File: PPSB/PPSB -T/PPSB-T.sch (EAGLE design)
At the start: 7 parts, among them U1 DS18B20

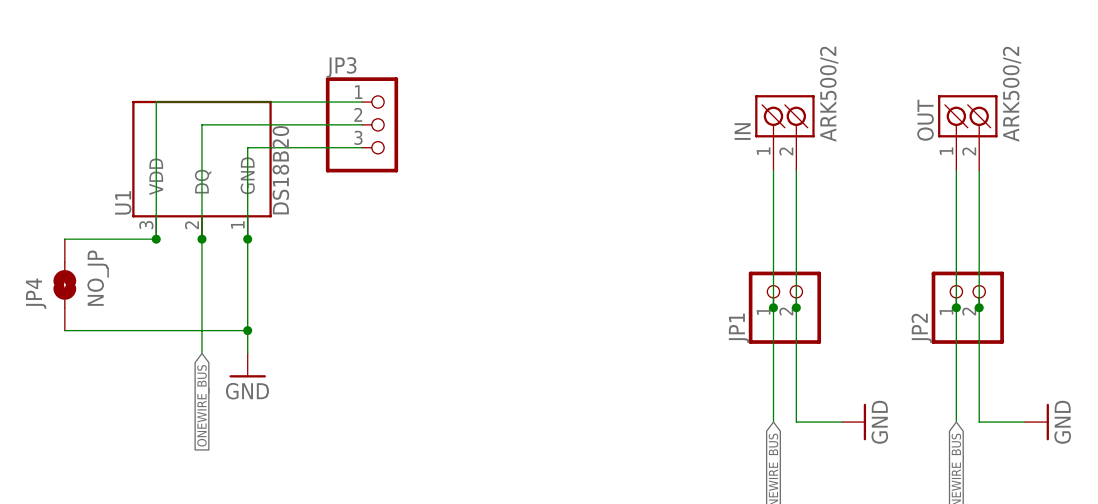
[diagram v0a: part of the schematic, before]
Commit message: Remove obsolete files, pre-release versions of PPSB-T & PPSB-TH
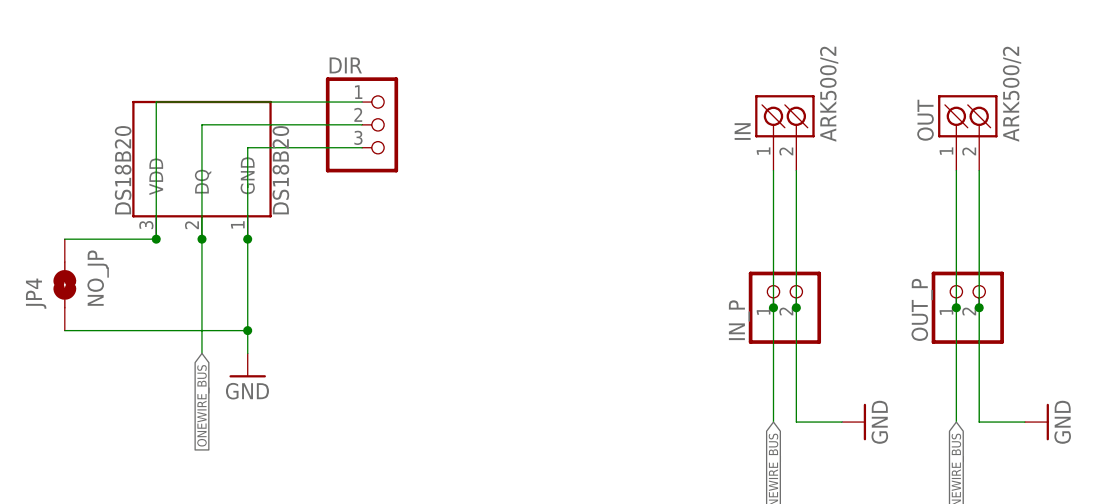
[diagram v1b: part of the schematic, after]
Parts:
- renumbered JP1 to IN_P, JP2 to OUT_P, JP3 to DIR, U1 to DS18B20
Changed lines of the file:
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@@
 <?xml version="1.0" encoding="utf-8"?>
 <!DOCTYPE eagle SYSTEM "eagle.dtd">
-<eagle version="9.5.2">
+<eagle version="9.6.1">
 <drawing>
 <settings>
@@
 <setting verticaltext="up"/>
 </settings>
-<grid distance="0.1" unitdist="inch" unit="inch" style="lines" multiple="1" display="yes" altdistance="0.01" altunitdist="inch" altunit="inch"/>
+<grid distance="0.1" unitdist="inch" unit="inch" style="lines" multiple="1" display="no" altdistance="0.01" altunitdist="inch" altunit="inch"/>
 <layers>
 <layer number="1" name="Top" color="4" fill="1" visible="no" active="no"/>
@@
 <parts>
 <part name="FRAME1" library="frames" library_urn="urn:adsk.eagle:library:229" deviceset="A4L-LOC" device=""/>
-<part name="U1" library="SparkFun-Sensors" deviceset="DS18B20" device=""/>
+<part name="DS18B20" library="SparkFun-Sensors" deviceset="DS18B20" device=""/>
 <part name="GND1" library="supply1" library_urn="urn:adsk.eagle:library:371" deviceset="GND" device=""/>
 <part name="IN" library="#PaJa_konektory" deviceset="ARK500/2" device=""/>
 <part name="OUT" library="#PaJa_konektory" deviceset="ARK500/2" device=""/>
-<part name="JP1" library="pinhead" library_urn="urn:adsk.eagle:library:325" deviceset="PINHD-1X2" device="" package3d_urn="urn:adsk.eagle:package:22435/2"/>
-<part name="JP2" library="pinhead" library_urn="urn:adsk.eagle:library:325" deviceset="PINHD-1X2" device="" package3d_urn="urn:adsk.eagle:package:22435/2"/>
+<part name="IN_P" library="pinhead" library_urn="urn:adsk.eagle:library:325" deviceset="PINHD-1X2" device="" package3d_urn="urn:adsk.eagle:package:22435/2"/>
+<part name="OUT_P" library="pinhead" library_urn="urn:adsk.eagle:library:325" deviceset="PINHD-1X2" device="" package3d_urn="urn:adsk.eagle:package:22435/2"/>
 <part name="GND3" library="supply1" library_urn="urn:adsk.eagle:library:371" deviceset="GND" device=""/>
 <part name="GND2" library="supply1" library_urn="urn:adsk.eagle:library:371" deviceset="GND" device=""/>
-<part name="JP3" library="pinhead" library_urn="urn:adsk.eagle:library:325" deviceset="PINHD-1X3" device="" package3d_urn="urn:adsk.eagle:package:22458/2"/>
+<part name="DIR" library="pinhead" library_urn="urn:adsk.eagle:library:325" deviceset="PINHD-1X3" device="" package3d_urn="urn:adsk.eagle:package:22458/2"/>
 <part name="JP4" library="SparkFun-Jumpers" deviceset="JUMPER-SMT_2_NO" device="_NO-SILK" package3d_urn="urn:adsk.eagle:package:39277/1" value="NO_JP"/>
 </parts>
@@
 <attribute name="SHEET" x="230.505" y="5.08" size="2.54" layer="94"/>
 </instance>
-<instance part="U1" gate="G$1" x="58.42" y="134.62" smashed="yes" rot="R90">
+<instance part="DS18B20" gate="G$1" x="58.42" y="134.62" smashed="yes" rot="R90">
 <attribute name="NAME" x="50.546" y="127" size="1.778" layer="95" font="vector" rot="R90"/>
 <attribute name="VALUE" x="66.294" y="127" size="1.778" layer="96" font="vector" rot="R90" align="top-left"/>
@@
 <attribute name="VALUE" x="149.219" y="135.2735" size="1.778" layer="96" rot="R90"/>
 </instance>
-<instance part="JP1" gate="G$1" x="124.46" y="119.38" smashed="yes" rot="R90">
+<instance part="IN_P" gate="G$1" x="124.46" y="119.38" smashed="yes" rot="R90">
 <attribute name="NAME" x="118.745" y="113.03" size="1.778" layer="95" rot="R90"/>
 <attribute name="VALUE" x="129.54" y="113.03" size="1.778" layer="96" rot="R90"/>
 </instance>
-<instance part="JP2" gate="G$1" x="144.78" y="119.38" smashed="yes" rot="R90">
+<instance part="OUT_P" gate="G$1" x="144.78" y="119.38" smashed="yes" rot="R90">
 <attribute name="NAME" x="139.065" y="113.03" size="1.778" layer="95" rot="R90"/>
 <attribute name="VALUE" x="149.86" y="113.03" size="1.778" layer="96" rot="R90"/>
@@
 <attribute name="VALUE" x="134.62" y="101.6" size="1.778" layer="96" rot="R90"/>
 </instance>
-<instance part="JP3" gate="A" x="78.74" y="137.16" smashed="yes">
+<instance part="DIR" gate="A" x="78.74" y="137.16" smashed="yes">
 <attribute name="NAME" x="72.39" y="142.875" size="1.778" layer="95"/>
 <attribute name="VALUE" x="72.39" y="129.54" size="1.778" layer="96"/>
@@
 <net name="GND" class="0">
 <segment>
-<pinref part="JP3" gate="A" pin="3"/>
+<pinref part="DIR" gate="A" pin="3"/>
 <wire x1="63.5" y1="134.62" x2="76.2" y2="134.62" width="0.1524" layer="91"/>
-<pinref part="U1" gate="G$1" pin="GND"/>
+<pinref part="DS18B20" gate="G$1" pin="GND"/>
 <wire x1="63.5" y1="124.46" x2="63.5" y2="134.62" width="0.1524" layer="91"/>
 <junction x="63.5" y="124.46"/>
@@
 <segment>
 <pinref part="OUT" gate="K" pin="K2"/>
-<pinref part="JP2" gate="G$1" pin="2"/>
+<pinref part="OUT_P" gate="G$1" pin="2"/>
 <wire x1="144.78" y1="132.08" x2="144.78" y2="116.84" width="0.1524" layer="91"/>
 <wire x1="144.78" y1="116.84" x2="144.78" y2="104.14" width="0.1524" layer="91"/>
@@
 <segment>
 <pinref part="IN" gate="K" pin="K2"/>
-<pinref part="JP1" gate="G$1" pin="2"/>
+<pinref part="IN_P" gate="G$1" pin="2"/>
 <wire x1="124.46" y1="132.08" x2="124.46" y2="116.84" width="0.1524" layer="91"/>
 <wire x1="124.46" y1="116.84" x2="124.46" y2="104.14" width="0.1524" layer="91"/>
@@
 <net name="ONEWIRE_BUS" class="0">
 <segment>
-<pinref part="U1" gate="G$1" pin="DQ"/>
+<pinref part="DS18B20" gate="G$1" pin="DQ"/>
 <wire x1="58.42" y1="124.46" x2="58.42" y2="111.76" width="0.1524" layer="91"/>
 <label x="58.42" y="111.76" size="1.016" layer="95" rot="R270" xref="yes"/>
 <wire x1="58.42" y1="124.46" x2="58.42" y2="137.16" width="0.1524" layer="91"/>
 <junction x="58.42" y="124.46"/>
-<pinref part="JP3" gate="A" pin="2"/>
+<pinref part="DIR" gate="A" pin="2"/>
 <wire x1="58.42" y1="137.16" x2="76.2" y2="137.16" width="0.1524" layer="91"/>
 </segment>
 <segment>
 <pinref part="IN" gate="K" pin="K1"/>
-<pinref part="JP1" gate="G$1" pin="1"/>
+<pinref part="IN_P" gate="G$1" pin="1"/>
 <wire x1="121.92" y1="132.08" x2="121.92" y2="116.84" width="0.1524" layer="91"/>
 <wire x1="121.92" y1="116.84" x2="121.92" y2="104.14" width="0.1524" layer="91"/>
@@
 <segment>
 <pinref part="OUT" gate="K" pin="K1"/>
-<pinref part="JP2" gate="G$1" pin="1"/>
+<pinref part="OUT_P" gate="G$1" pin="1"/>
 <wire x1="142.24" y1="132.08" x2="142.24" y2="116.84" width="0.1524" layer="91"/>
 <wire x1="142.24" y1="116.84" x2="142.24" y2="104.14" width="0.1524" layer="91"/>
@@
 <net name="N$1" class="0">
 <segment>
-<pinref part="JP3" gate="A" pin="1"/>
+<pinref part="DIR" gate="A" pin="1"/>
 <wire x1="53.34" y1="139.7" x2="76.2" y2="139.7" width="0.1524" layer="91"/>
-<pinref part="U1" gate="G$1" pin="VDD"/>
+<pinref part="DS18B20" gate="G$1" pin="VDD"/>
 <wire x1="53.34" y1="124.46" x2="53.34" y2="139.7" width="0.1524" layer="91"/>
 <pinref part="JP4" gate="G$1" pin="2"/>

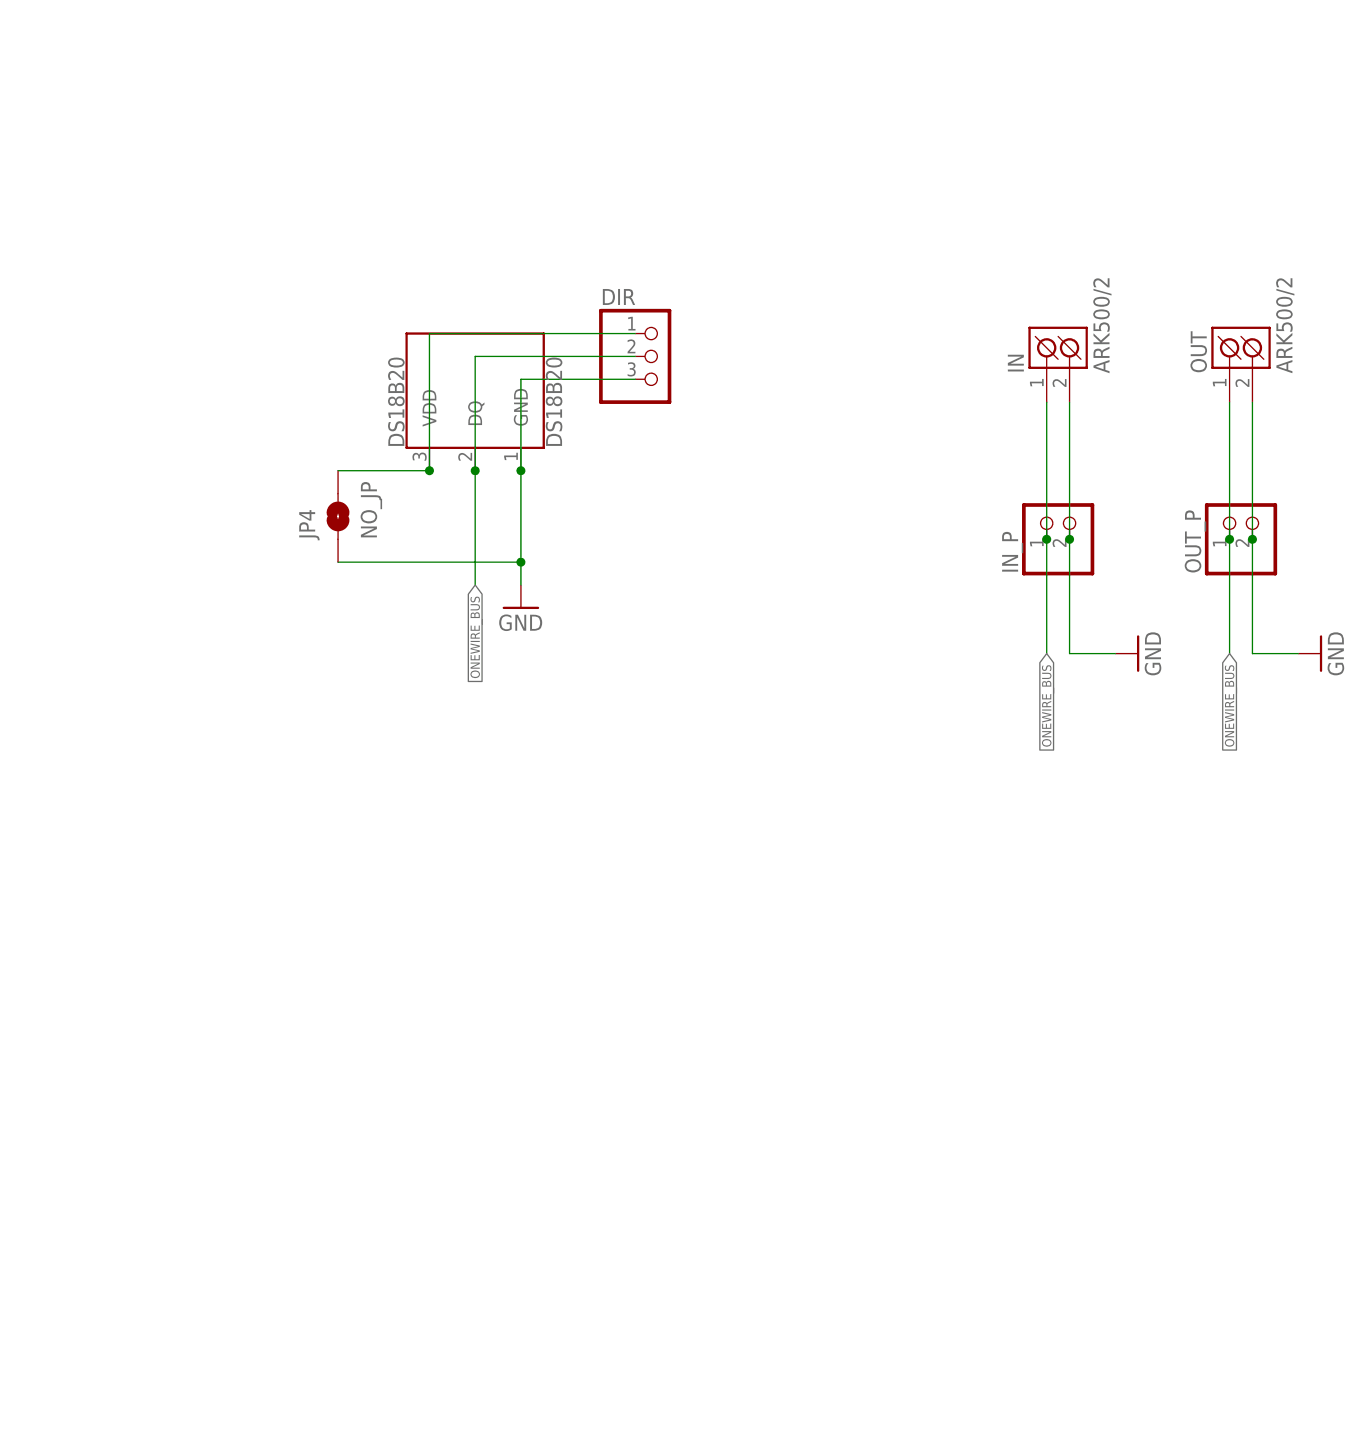
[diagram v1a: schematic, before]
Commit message: Improved schematics layout.
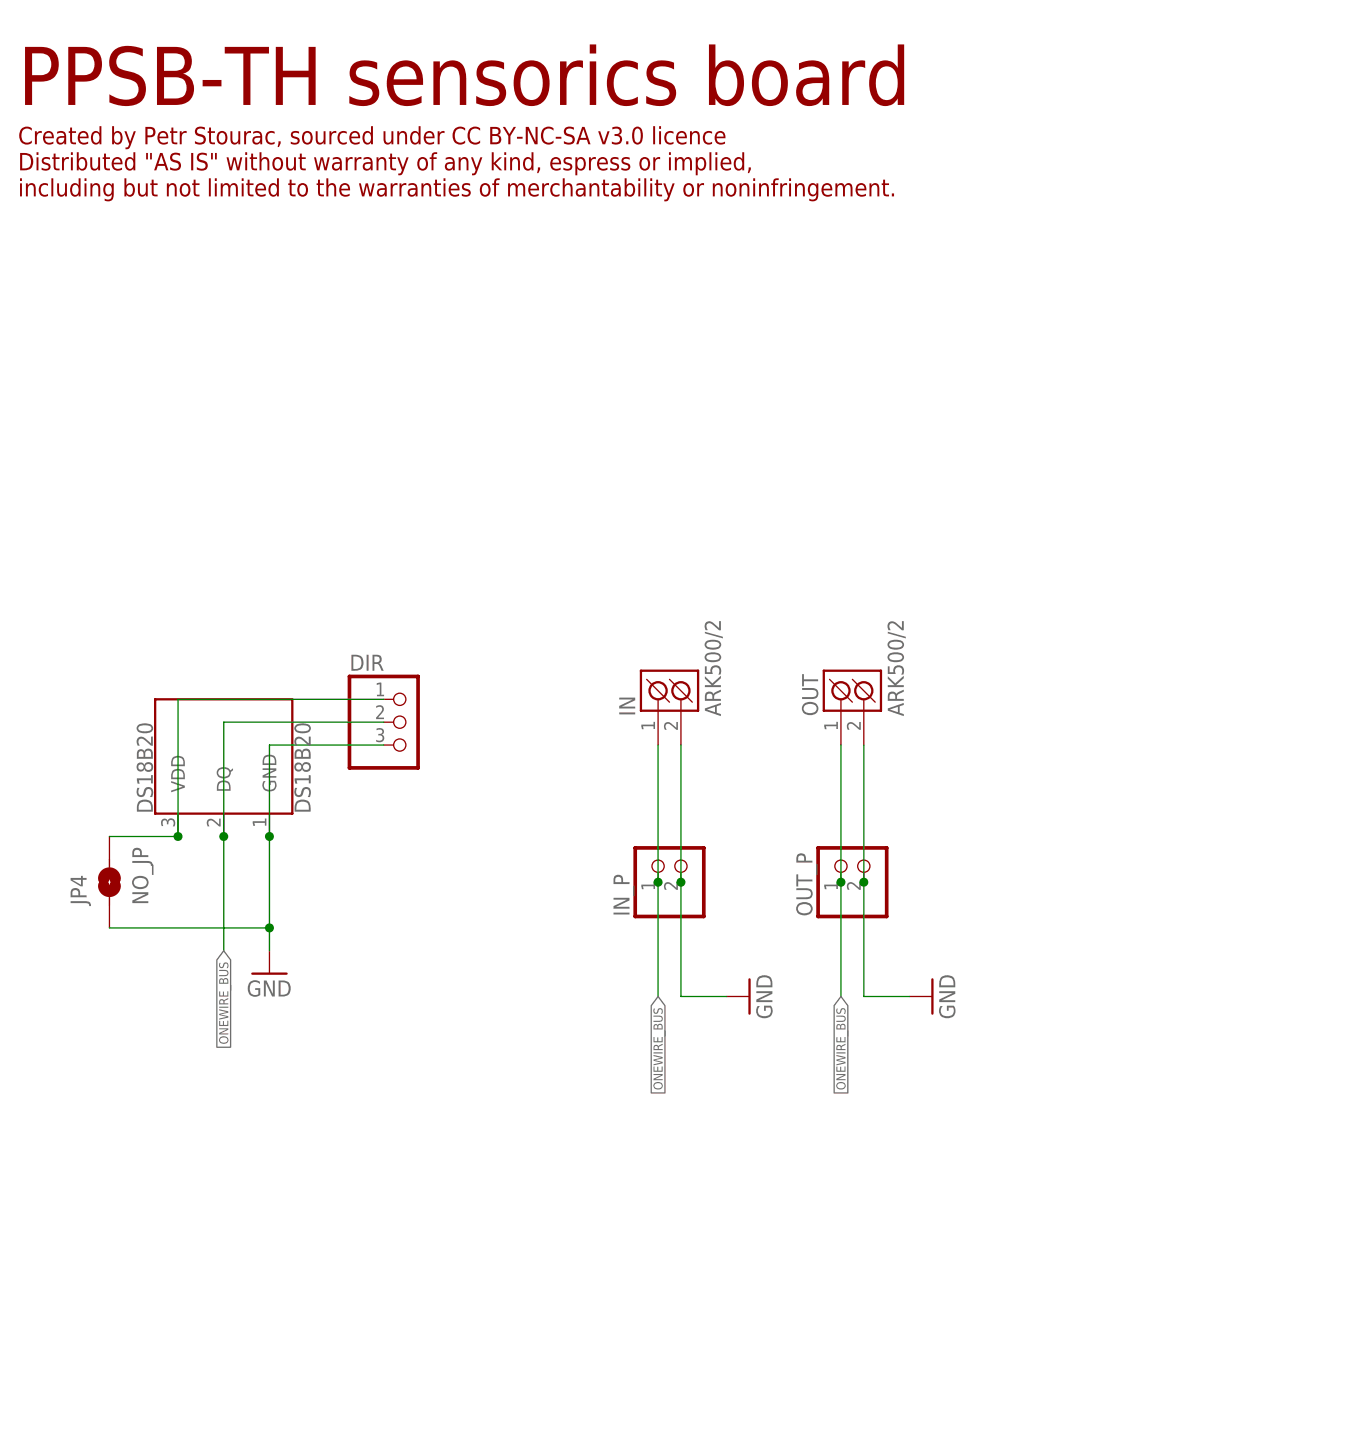
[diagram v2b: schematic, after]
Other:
- note added: "Created by Petr Stourac, sourced under CC BY-NC-SA v3.0 licence Distributed "AS IS" without warranty of any kind, espress or implied, including but not limited to the warranties of merchantability or noninfringement."
- note added: "PPSB-TH sensorics board"
- moved on the sheet: DIR, DS18B20, IN, IN_P, JP4, OUT, OUT_P

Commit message: Update schematics
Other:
- note added: "ver. 1 rev. 1"
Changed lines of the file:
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@@
 <setting verticaltext="up"/>
 </settings>
-<grid distance="0.1" unitdist="inch" unit="inch" style="lines" multiple="1" display="yes" altdistance="0.01" altunitdist="inch" altunit="inch"/>
+<grid distance="0.1" unitdist="inch" unit="inch" style="lines" multiple="1" display="no" altdistance="0.01" altunitdist="inch" altunit="inch"/>
 <layers>
 <layer number="1" name="Top" color="4" fill="1" visible="no" active="no"/>
@@
 Distributed "AS IS" without warranty of any kind, espress or implied,
 including but not limited to the warranties of merchantability or noninfringement.</text>
+<text x="87.63" y="20.32" size="2.54" layer="94">ver. 1 rev. 1</text>
 </plain>
 <instances>
